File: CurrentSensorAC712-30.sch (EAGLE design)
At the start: 1 part, among them U1 ACS712ELCTR30AT

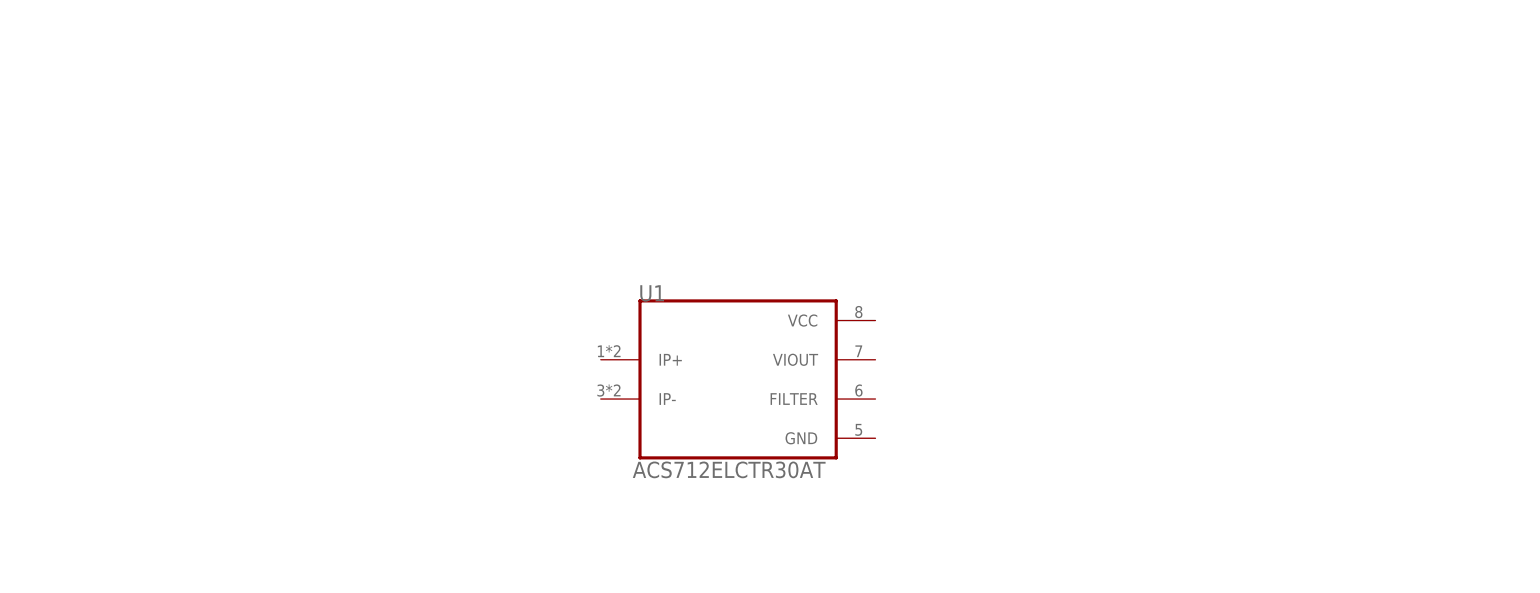
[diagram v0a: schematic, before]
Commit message: current sensor got some r and c
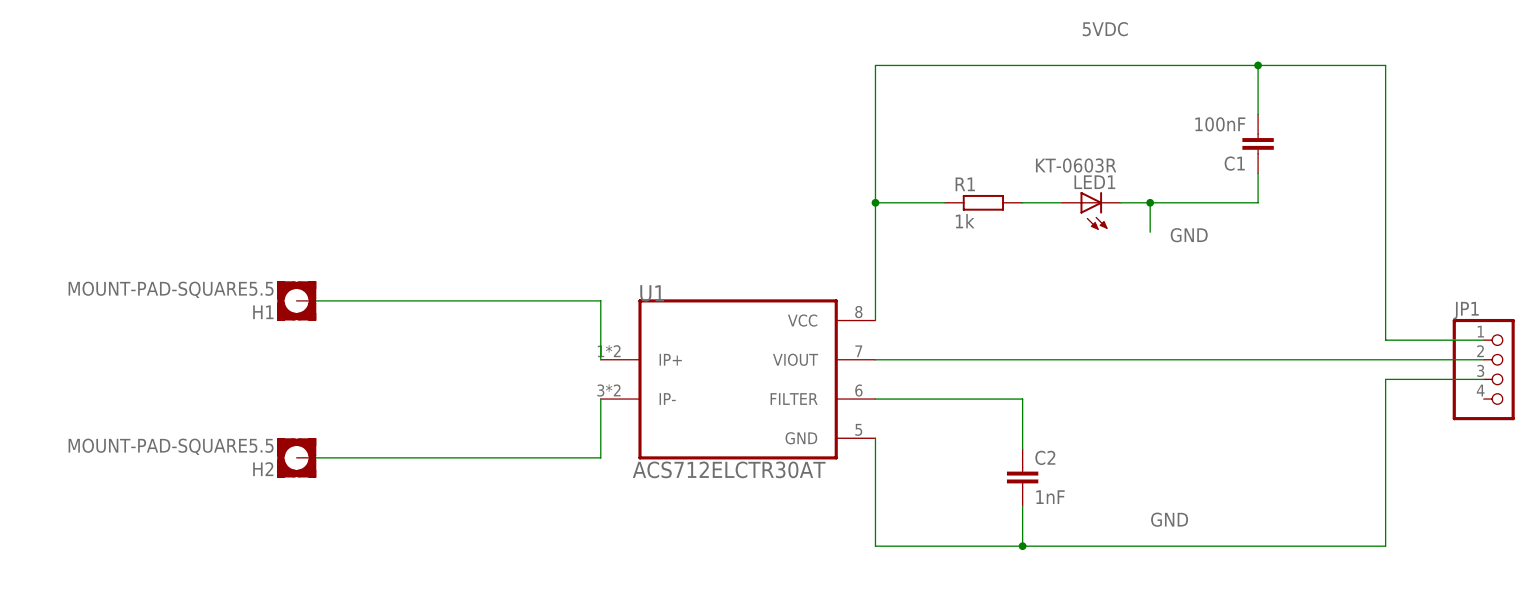
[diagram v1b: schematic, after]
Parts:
- added C1: 100nF, rcl:C-EUC0805
- added C2: 1nF, rcl:C-EUC0805
- added H1, H2: MOUNT-PAD-SQUARE5.5, holes:MOUNT-PAD-SQUARE5.5
- added JP1: (no value), pinhead:PINHD-1X4/90
- added LED1: KT-0603R, led:LEDCHIPLED_0603
- added R1: 1k, rcl:R-EU_R0805
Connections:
- new net 5VDC: C1.2, JP1.1, R1.1, U1.VCC
- new net GND: C1.1, C2.2, JP1.3, LED1.C, U1.GND
- new net N$1: H1.MOUNT, U1.IP+
- new net N$2: H2.MOUNT, U1.IP-
- new net N$4: C2.1, U1.FILTER
- new net N$5: LED1.A, R1.2
- new net N$6: JP1.2, U1.VIOUT
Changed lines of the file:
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@@
 <setting verticaltext="up"/>
 </settings>
-<grid distance="0.1" unitdist="inch" unit="inch" style="lines" multiple="1" display="no" altdistance="0.01" altunitdist="inch" altunit="inch"/>
+<grid distance="50" unitdist="mil" unit="mil" style="lines" multiple="1" display="yes" altdistance="0.01" altunitdist="inch" altunit="inch"/>
 <layers>
 <layer number="1" name="Top" color="4" fill="1" visible="no" active="no"/>
@@
 <parts>
 <part name="U1" library="ACS712ELCTR30AT" deviceset="ACS712ELCTR30AT" device=""/>
+<part name="H1" library="holes" library_urn="urn:adsk.eagle:library:237" deviceset="MOUNT-PAD-SQUARE" device="5.5" package3d_urn="urn:adsk.eagle:package:14299/1"/>
+<part name="H2" library="holes" library_urn="urn:adsk.eagle:library:237" deviceset="MOUNT-PAD-SQUARE" device="5.5" package3d_urn="urn:adsk.eagle:package:14299/1"/>
+<part name="R1" library="rcl" library_urn="urn:adsk.eagle:library:334" deviceset="R-EU_" device="R0805" package3d_urn="urn:adsk.eagle:package:23553/2" value="1k"/>
+<part name="C1" library="rcl" library_urn="urn:adsk.eagle:library:334" deviceset="C-EU" device="C0805" package3d_urn="urn:adsk.eagle:package:23617/2" value="100nF"/>
+<part name="C2" library="rcl" library_urn="urn:adsk.eagle:library:334" deviceset="C-EU" device="C0805" package3d_urn="urn:adsk.eagle:package:23617/2" value="1nF"/>
+<part name="LED1" library="led" library_urn="urn:adsk.eagle:library:259" deviceset="LED" device="CHIPLED_0603" package3d_urn="urn:adsk.eagle:package:15822/1" value="KT-0603R"/>
+<part name="JP1" library="pinhead" library_urn="urn:adsk.eagle:library:325" deviceset="PINHD-1X4" device="/90" package3d_urn="urn:adsk.eagle:package:22404/1"/>
 </parts>
 <sheets>
@@
 <attribute name="VALUE" x="71.4424" y="49.4731" size="2.08746875" layer="96" ratio="10" rot="SR0"/>
 </instance>
+<instance part="H1" gate="G$1" x="27.94" y="72.39" smashed="yes" rot="R180">
+<attribute name="NAME" x="25.146" y="71.8058" size="1.778" layer="95" rot="R180"/>
+<attribute name="VALUE" x="25.146" y="74.8538" size="1.778" layer="96" rot="R180"/>
+</instance>
+<instance part="H2" gate="G$1" x="27.94" y="52.07" smashed="yes" rot="R180">
+<attribute name="NAME" x="25.146" y="51.4858" size="1.778" layer="95" rot="R180"/>
+<attribute name="VALUE" x="25.146" y="54.5338" size="1.778" layer="96" rot="R180"/>
+</instance>
+<instance part="R1" gate="G$1" x="116.84" y="85.09" smashed="yes">
+<attribute name="NAME" x="113.03" y="86.5886" size="1.778" layer="95"/>
+<attribute name="VALUE" x="113.03" y="81.788" size="1.778" layer="96"/>
+</instance>
+<instance part="C1" gate="G$1" x="152.4" y="91.44" smashed="yes" rot="R180">
+<attribute name="NAME" x="150.876" y="91.059" size="1.778" layer="95" rot="R180"/>
+<attribute name="VALUE" x="150.876" y="96.139" size="1.778" layer="96" rot="R180"/>
+</instance>
+<instance part="C2" gate="G$1" x="121.92" y="50.8" smashed="yes">
+<attribute name="NAME" x="123.444" y="51.181" size="1.778" layer="95"/>
+<attribute name="VALUE" x="123.444" y="46.101" size="1.778" layer="96"/>
+</instance>
+<instance part="LED1" gate="G$1" x="129.54" y="85.09" smashed="yes" rot="R90">
+<attribute name="NAME" x="134.112" y="88.646" size="1.778" layer="95" rot="R180"/>
+<attribute name="VALUE" x="134.112" y="90.805" size="1.778" layer="96" rot="R180"/>
+</instance>
+<instance part="JP1" gate="A" x="184.15" y="62.23" smashed="yes">
+<attribute name="NAME" x="177.8" y="70.485" size="1.778" layer="95"/>
+<attribute name="VALUE" x="177.8" y="54.61" size="1.778" layer="96"/>
+</instance>
 </instances>
 <busses>
 </busses>
 <nets>
+<net name="N$1" class="0">
+<segment>
+<pinref part="U1" gate="G$1" pin="IP+"/>
+<pinref part="H1" gate="G$1" pin="MOUNT"/>
+<wire x1="67.31" y1="64.77" x2="67.31" y2="72.39" width="0.1524" layer="91"/>
+<wire x1="67.31" y1="72.39" x2="30.48" y2="72.39" width="0.1524" layer="91"/>
+</segment>
+</net>
+<net name="N$2" class="0">
+<segment>
+<pinref part="U1" gate="G$1" pin="IP-"/>
+<pinref part="H2" gate="G$1" pin="MOUNT"/>
+<wire x1="67.31" y1="59.69" x2="67.31" y2="52.07" width="0.1524" layer="91"/>
+<wire x1="67.31" y1="52.07" x2="30.48" y2="52.07" width="0.1524" layer="91"/>
+</segment>
+</net>
+<net name="5VDC" class="0">
+<segment>
+<wire x1="181.61" y1="67.31" x2="168.91" y2="67.31" width="0.1524" layer="91"/>
+<wire x1="168.91" y1="67.31" x2="168.91" y2="102.87" width="0.1524" layer="91"/>
+<pinref part="U1" gate="G$1" pin="VCC"/>
+<wire x1="168.91" y1="102.87" x2="152.4" y2="102.87" width="0.1524" layer="91"/>
+<wire x1="152.4" y1="102.87" x2="102.87" y2="102.87" width="0.1524" layer="91"/>
+<wire x1="102.87" y1="102.87" x2="102.87" y2="85.09" width="0.1524" layer="91"/>
+<pinref part="R1" gate="G$1" pin="1"/>
+<wire x1="102.87" y1="85.09" x2="102.87" y2="69.85" width="0.1524" layer="91"/>
+<wire x1="111.76" y1="85.09" x2="102.87" y2="85.09" width="0.1524" layer="91"/>
+<junction x="102.87" y="85.09"/>
+<pinref part="C1" gate="G$1" pin="2"/>
+<wire x1="152.4" y1="96.52" x2="152.4" y2="102.87" width="0.1524" layer="91"/>
+<junction x="152.4" y="102.87"/>
+<pinref part="JP1" gate="A" pin="1"/>
+<label x="129.54" y="106.68" size="1.778" layer="95"/>
+</segment>
+</net>
+<net name="N$5" class="0">
+<segment>
+<pinref part="LED1" gate="G$1" pin="A"/>
+<pinref part="R1" gate="G$1" pin="2"/>
+<wire x1="127" y1="85.09" x2="121.92" y2="85.09" width="0.1524" layer="91"/>
+</segment>
+</net>
+<net name="GND" class="0">
+<segment>
+<pinref part="LED1" gate="G$1" pin="C"/>
+<wire x1="134.62" y1="85.09" x2="138.43" y2="85.09" width="0.1524" layer="91"/>
+<wire x1="138.43" y1="85.09" x2="138.43" y2="81.28" width="0.1524" layer="91"/>
+<label x="140.97" y="80.01" size="1.778" layer="95"/>
+<wire x1="138.43" y1="85.09" x2="152.4" y2="85.09" width="0.1524" layer="91"/>
+<junction x="138.43" y="85.09"/>
+<wire x1="152.4" y1="85.09" x2="152.4" y2="88.9" width="0.1524" layer="91"/>
+<pinref part="C1" gate="G$1" pin="1"/>
+</segment>
+<segment>
+<pinref part="JP1" gate="A" pin="3"/>
+<wire x1="181.61" y1="62.23" x2="168.91" y2="62.23" width="0.1524" layer="91"/>
+<wire x1="168.91" y1="62.23" x2="168.91" y2="40.64" width="0.1524" layer="91"/>
+<pinref part="U1" gate="G$1" pin="GND"/>
+<wire x1="168.91" y1="40.64" x2="121.92" y2="40.64" width="0.1524" layer="91"/>
+<wire x1="121.92" y1="40.64" x2="102.87" y2="40.64" width="0.1524" layer="91"/>
+<wire x1="102.87" y1="40.64" x2="102.87" y2="54.61" width="0.1524" layer="91"/>
+<label x="138.43" y="43.18" size="1.778" layer="95"/>
+<pinref part="C2" gate="G$1" pin="2"/>
+<wire x1="121.92" y1="45.72" x2="121.92" y2="40.64" width="0.1524" layer="91"/>
+<junction x="121.92" y="40.64"/>
+</segment>
+</net>
+<net name="N$4" class="0">
+<segment>
+<wire x1="102.87" y1="59.69" x2="121.92" y2="59.69" width="0.1524" layer="91"/>
+<wire x1="121.92" y1="59.69" x2="121.92" y2="53.34" width="0.1524" layer="91"/>
+<pinref part="C2" gate="G$1" pin="1"/>
+<pinref part="U1" gate="G$1" pin="FILTER"/>
+</segment>
+</net>
+<net name="N$6" class="0">
+<segment>
+<pinref part="U1" gate="G$1" pin="VIOUT"/>
+<pinref part="JP1" gate="A" pin="2"/>
+<wire x1="102.87" y1="64.77" x2="181.61" y2="64.77" width="0.1524" layer="91"/>
+</segment>
+</net>
 </nets>
 </sheet>
@@
 </schematic>
 </drawing>
+<compatibility>
+<note version="8.2" severity="warning">
+Since Version 8.2, EAGLE supports online libraries. The ids
+of those online libraries will not be understood (or retained)
+with this version.
+</note>
+<note version="8.3" severity="warning">
+Since Version 8.3, EAGLE supports URNs for individual library
+assets (packages, symbols, and devices). The URNs of those assets
+will not be understood (or retained) with this version.
+</note>
+<note version="8.3" severity="warning">
+Since Version 8.3, EAGLE supports the association of 3D packages
+with devices in libraries, schematics, and board files. Those 3D
+packages will not be understood (or retained) with this version.
+</note>
+</compatibility>
 </eagle>

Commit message: current sensor layouted
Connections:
- net N$1 renamed IN
- net N$2 renamed OUT
- net GND: now also JP1.4
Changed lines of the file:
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@@
 </busses>
 <nets>
-<net name="N$1" class="0">
+<net name="IN" class="0">
 <segment>
 <pinref part="U1" gate="G$1" pin="IP+"/>
@@
 <wire x1="67.31" y1="64.77" x2="67.31" y2="72.39" width="0.1524" layer="91"/>
 <wire x1="67.31" y1="72.39" x2="30.48" y2="72.39" width="0.1524" layer="91"/>
+<label x="45.72" y="74.93" size="1.778" layer="95"/>
 </segment>
 </net>
-<net name="N$2" class="0">
+<net name="OUT" class="0">
 <segment>
 <pinref part="U1" gate="G$1" pin="IP-"/>
@@
 <wire x1="67.31" y1="59.69" x2="67.31" y2="52.07" width="0.1524" layer="91"/>
 <wire x1="67.31" y1="52.07" x2="30.48" y2="52.07" width="0.1524" layer="91"/>
+<label x="46.99" y="49.53" size="1.778" layer="95"/>
 </segment>
 </net>
@@
 <wire x1="121.92" y1="45.72" x2="121.92" y2="40.64" width="0.1524" layer="91"/>
 <junction x="121.92" y="40.64"/>
+<pinref part="JP1" gate="A" pin="4"/>
+<wire x1="181.61" y1="59.69" x2="181.61" y2="62.23" width="0.1524" layer="91"/>
+<junction x="181.61" y="62.23"/>
 </segment>
 </net>

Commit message: new extension board design used
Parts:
- removed H1, H2: MOUNT-PAD-SQUARE5.5, holes:MOUNT-PAD-SQUARE5.5
- added JP2: (no value), pinhead:PINHD-1X5
- JP1: device pinhead:PINHD-1X4/90 -> pinhead:PINHD-1X5
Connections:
- net 5VDC: now also JP1.2
- net GND: now also JP1.5; no longer JP1.3
- net IN: no longer H1.MOUNT
- net N$6: now also JP1.3; no longer JP1.2
- net OUT: no longer H2.MOUNT
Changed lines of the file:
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@@
 <parts>
 <part name="U1" library="ACS712ELCTR30AT" deviceset="ACS712ELCTR30AT" device=""/>
-<part name="H1" library="holes" library_urn="urn:adsk.eagle:library:237" deviceset="MOUNT-PAD-SQUARE" device="5.5" package3d_urn="urn:adsk.eagle:package:14299/1"/>
-<part name="H2" library="holes" library_urn="urn:adsk.eagle:library:237" deviceset="MOUNT-PAD-SQUARE" device="5.5" package3d_urn="urn:adsk.eagle:package:14299/1"/>
 <part name="R1" library="rcl" library_urn="urn:adsk.eagle:library:334" deviceset="R-EU_" device="R0805" package3d_urn="urn:adsk.eagle:package:23553/2" value="1k"/>
 <part name="C1" library="rcl" library_urn="urn:adsk.eagle:library:334" deviceset="C-EU" device="C0805" package3d_urn="urn:adsk.eagle:package:23617/2" value="100nF"/>
 <part name="C2" library="rcl" library_urn="urn:adsk.eagle:library:334" deviceset="C-EU" device="C0805" package3d_urn="urn:adsk.eagle:package:23617/2" value="1nF"/>
 <part name="LED1" library="led" library_urn="urn:adsk.eagle:library:259" deviceset="LED" device="CHIPLED_0603" package3d_urn="urn:adsk.eagle:package:15822/1" value="KT-0603R"/>
-<part name="JP1" library="pinhead" library_urn="urn:adsk.eagle:library:325" deviceset="PINHD-1X4" device="/90" package3d_urn="urn:adsk.eagle:package:22404/1"/>
+<part name="JP1" library="pinhead" library_urn="urn:adsk.eagle:library:325" deviceset="PINHD-1X5" device="" package3d_urn="urn:adsk.eagle:package:22469/2"/>
+<part name="JP2" library="pinhead" library_urn="urn:adsk.eagle:library:325" deviceset="PINHD-1X5" device="" package3d_urn="urn:adsk.eagle:package:22469/2"/>
 </parts>
 <sheets>
@@
 <attribute name="NAME" x="72.2036" y="72.3387" size="2.08621875" layer="95" ratio="10" rot="SR0"/>
 <attribute name="VALUE" x="71.4424" y="49.4731" size="2.08746875" layer="96" ratio="10" rot="SR0"/>
-</instance>
-<instance part="H1" gate="G$1" x="27.94" y="72.39" smashed="yes" rot="R180">
-<attribute name="NAME" x="25.146" y="71.8058" size="1.778" layer="95" rot="R180"/>
-<attribute name="VALUE" x="25.146" y="74.8538" size="1.778" layer="96" rot="R180"/>
-</instance>
-<instance part="H2" gate="G$1" x="27.94" y="52.07" smashed="yes" rot="R180">
-<attribute name="NAME" x="25.146" y="51.4858" size="1.778" layer="95" rot="R180"/>
-<attribute name="VALUE" x="25.146" y="54.5338" size="1.778" layer="96" rot="R180"/>
 </instance>
 <instance part="R1" gate="G$1" x="116.84" y="85.09" smashed="yes">
@@
 <attribute name="VALUE" x="134.112" y="90.805" size="1.778" layer="96" rot="R180"/>
 </instance>
-<instance part="JP1" gate="A" x="184.15" y="62.23" smashed="yes">
-<attribute name="NAME" x="177.8" y="70.485" size="1.778" layer="95"/>
-<attribute name="VALUE" x="177.8" y="54.61" size="1.778" layer="96"/>
+<instance part="JP1" gate="A" x="185.42" y="64.77" smashed="yes">
+<attribute name="NAME" x="179.07" y="73.025" size="1.778" layer="95"/>
+<attribute name="VALUE" x="179.07" y="54.61" size="1.778" layer="96"/>
+</instance>
+<instance part="JP2" gate="A" x="185.42" y="44.45" smashed="yes">
+<attribute name="NAME" x="179.07" y="52.705" size="1.778" layer="95"/>
+<attribute name="VALUE" x="179.07" y="34.29" size="1.778" layer="96"/>
 </instance>
 </instances>
@@
 <segment>
 <pinref part="U1" gate="G$1" pin="IP+"/>
-<pinref part="H1" gate="G$1" pin="MOUNT"/>
 <wire x1="67.31" y1="64.77" x2="67.31" y2="72.39" width="0.1524" layer="91"/>
 <wire x1="67.31" y1="72.39" x2="30.48" y2="72.39" width="0.1524" layer="91"/>
@@
 <segment>
 <pinref part="U1" gate="G$1" pin="IP-"/>
-<pinref part="H2" gate="G$1" pin="MOUNT"/>
 <wire x1="67.31" y1="59.69" x2="67.31" y2="52.07" width="0.1524" layer="91"/>
 <wire x1="67.31" y1="52.07" x2="30.48" y2="52.07" width="0.1524" layer="91"/>
@@
 <net name="5VDC" class="0">
 <segment>
-<wire x1="181.61" y1="67.31" x2="168.91" y2="67.31" width="0.1524" layer="91"/>
+<wire x1="182.88" y1="67.31" x2="168.91" y2="67.31" width="0.1524" layer="91"/>
 <wire x1="168.91" y1="67.31" x2="168.91" y2="102.87" width="0.1524" layer="91"/>
 <pinref part="U1" gate="G$1" pin="VCC"/>
@@
 <wire x1="152.4" y1="96.52" x2="152.4" y2="102.87" width="0.1524" layer="91"/>
 <junction x="152.4" y="102.87"/>
+<label x="129.54" y="106.68" size="1.778" layer="95"/>
+<pinref part="JP1" gate="A" pin="2"/>
 <pinref part="JP1" gate="A" pin="1"/>
-<label x="129.54" y="106.68" size="1.778" layer="95"/>
+<wire x1="182.88" y1="67.31" x2="182.88" y2="69.85" width="0.1524" layer="91"/>
+<junction x="182.88" y="67.31"/>
 </segment>
 </net>
@@
 </segment>
 <segment>
-<pinref part="JP1" gate="A" pin="3"/>
 <wire x1="181.61" y1="62.23" x2="168.91" y2="62.23" width="0.1524" layer="91"/>
 <wire x1="168.91" y1="62.23" x2="168.91" y2="40.64" width="0.1524" layer="91"/>
@@
 <wire x1="121.92" y1="45.72" x2="121.92" y2="40.64" width="0.1524" layer="91"/>
 <junction x="121.92" y="40.64"/>
+<wire x1="181.61" y1="59.69" x2="181.61" y2="62.23" width="0.1524" layer="91"/>
+<pinref part="JP1" gate="A" pin="5"/>
+<wire x1="181.61" y1="59.69" x2="182.88" y2="59.69" width="0.1524" layer="91"/>
 <pinref part="JP1" gate="A" pin="4"/>
-<wire x1="181.61" y1="59.69" x2="181.61" y2="62.23" width="0.1524" layer="91"/>
+<wire x1="182.88" y1="62.23" x2="181.61" y2="62.23" width="0.1524" layer="91"/>
 <junction x="181.61" y="62.23"/>
 </segment>
@@
 <segment>
 <pinref part="U1" gate="G$1" pin="VIOUT"/>
-<pinref part="JP1" gate="A" pin="2"/>
-<wire x1="102.87" y1="64.77" x2="181.61" y2="64.77" width="0.1524" layer="91"/>
+<wire x1="102.87" y1="64.77" x2="182.88" y2="64.77" width="0.1524" layer="91"/>
+<pinref part="JP1" gate="A" pin="3"/>
 </segment>
 </net>
